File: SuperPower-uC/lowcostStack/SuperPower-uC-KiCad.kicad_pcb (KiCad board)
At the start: 4 copper layers, 92.2 x 45.2 mm, 105 parts, among them J1 Battery connector, J10 External NTC, J11 DNP, J2 Thermistor, J3 USB_B_Micro, J4 Solar in, J5 Conn_01x14_Female, J6 Conn_01x14_Female, J7 DNP, J8 regulator board, J9 MCU board, Q1 2N7002, Q2 2N7002, Q3 S8050, Q4 S8050, Q5 AO3401A, Q6 AO3401A, Q7 2N7002, Q8 2N7002, Q9 AO3401A, SW1 DNP, SW2 DNP, U1 AP9101CK6-ADTRG1, U10 FP6291LR, U11 ME6210A33P, U12 ME6210A33P, U13 ESP32-WROOM32, U14 W25Q32JVSS, U15 IP4220CZ6, U2 FS8205A, U3 LC709203FQH, U4 TP4056, U5 CH340G, U6 AMS1117-3.3, U7 PCF8563T, U8 XC6206P332MR, U9 TCA6408A, Y1 12MHZ, Y2 32.768KHz

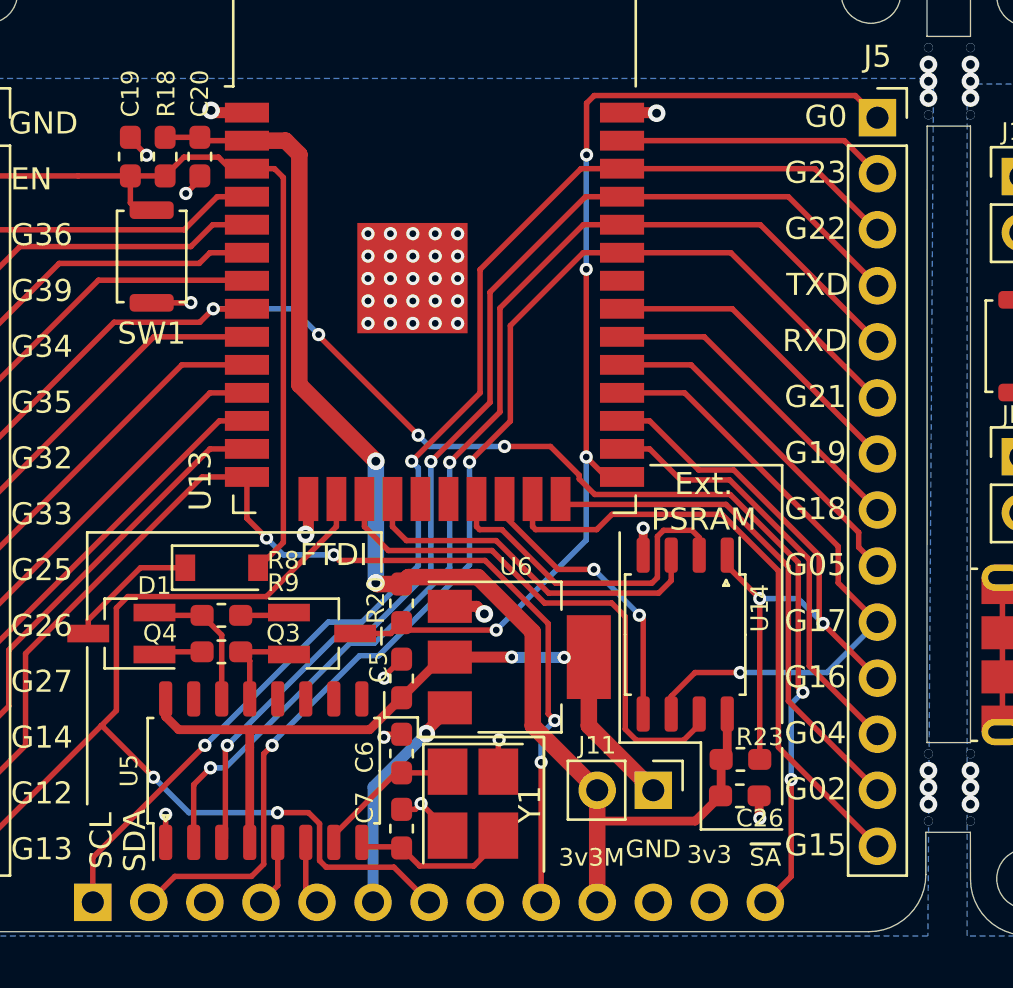
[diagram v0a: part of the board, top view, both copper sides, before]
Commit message: changed naming of usb to serial stuff and added led to mcu board
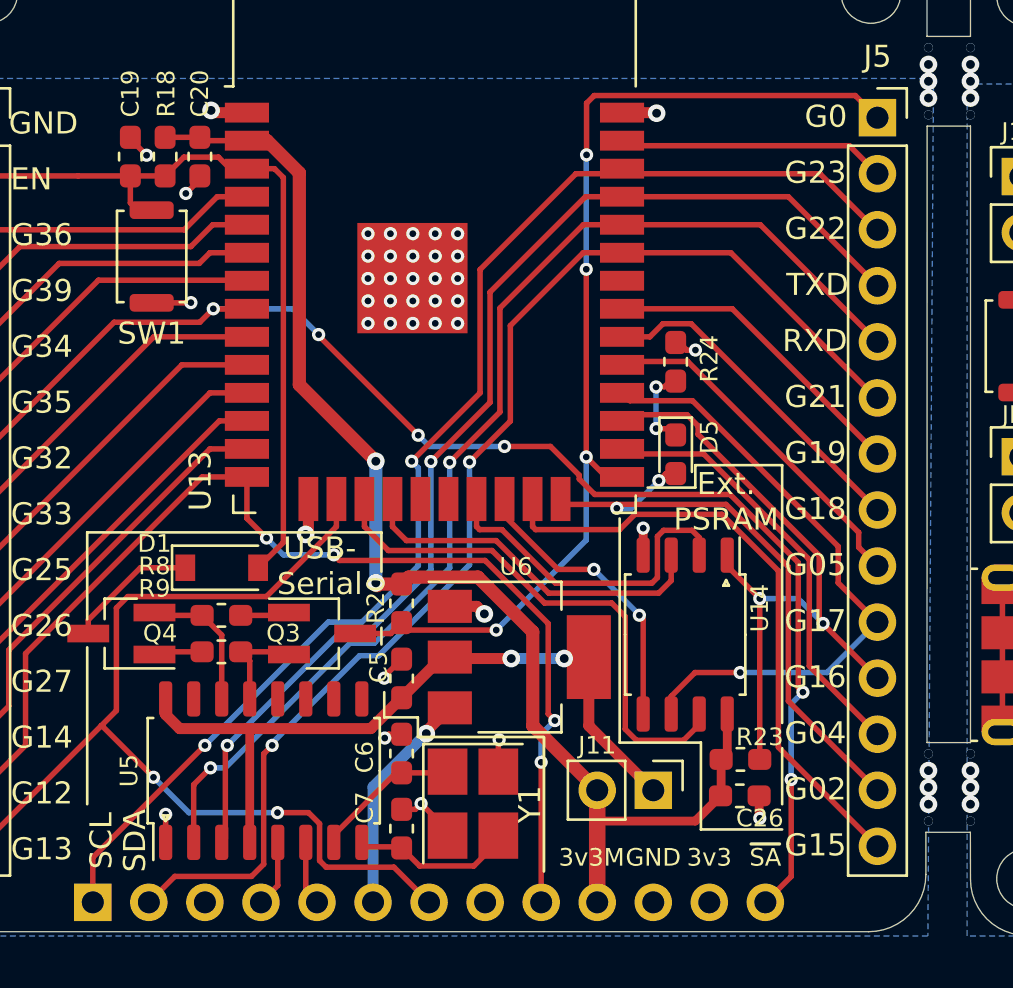
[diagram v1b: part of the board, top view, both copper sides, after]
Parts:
- added D5: LED, LED_SMD:LED_0603_1608Metric_Pad1.05x0.95mm_HandSolder, F.Cu at (135.4, 99.7)
- added R24: 100, Resistor_SMD:R_0603_1608Metric_Pad1.05x0.95mm_HandSolder, F.Cu at (135.4, 95.5)
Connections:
- net /MCU Module/3v3FTDI renamed /MCU Module/3v3_UART
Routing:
- net Net-(D5-Pad1): track 0.00 -> 3.89 mm, vias 0 -> 2
- net /MCU Module/IO2: track 23.8 -> 27.3 mm, vias 0 -> 2
- net GND: track 88.5 -> 89.6 mm, vias 80 -> 81
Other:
- board text added: "USB- Serial"
- board text removed: "FTDI"

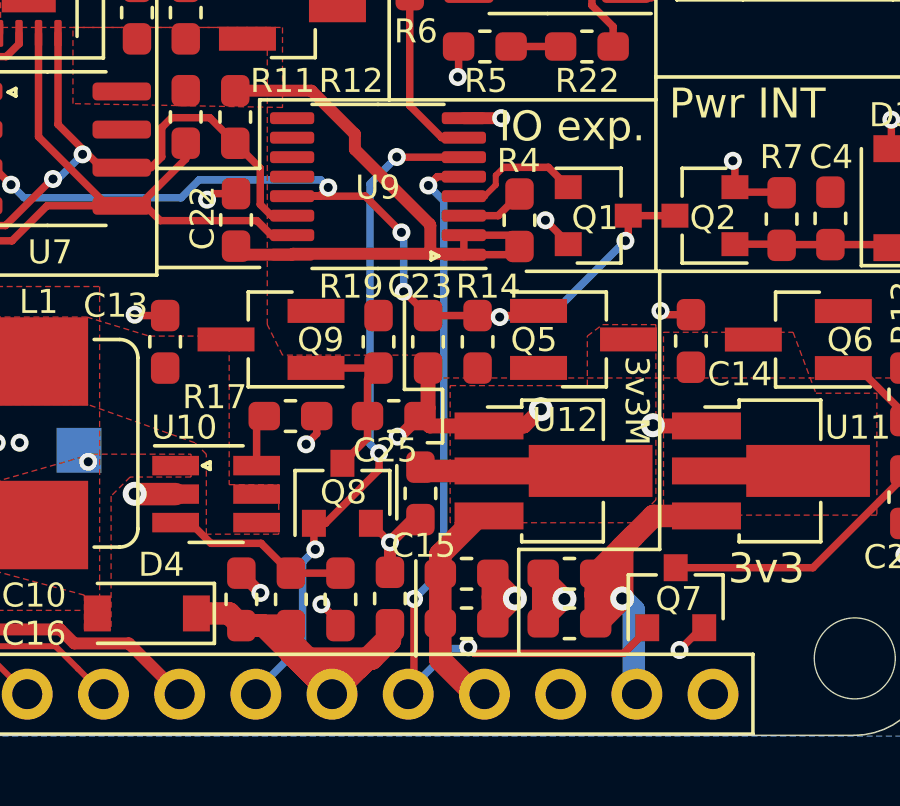
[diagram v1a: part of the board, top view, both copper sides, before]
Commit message: disconnected 5v_EN and 3v3_EN from the pin header on the regulator board
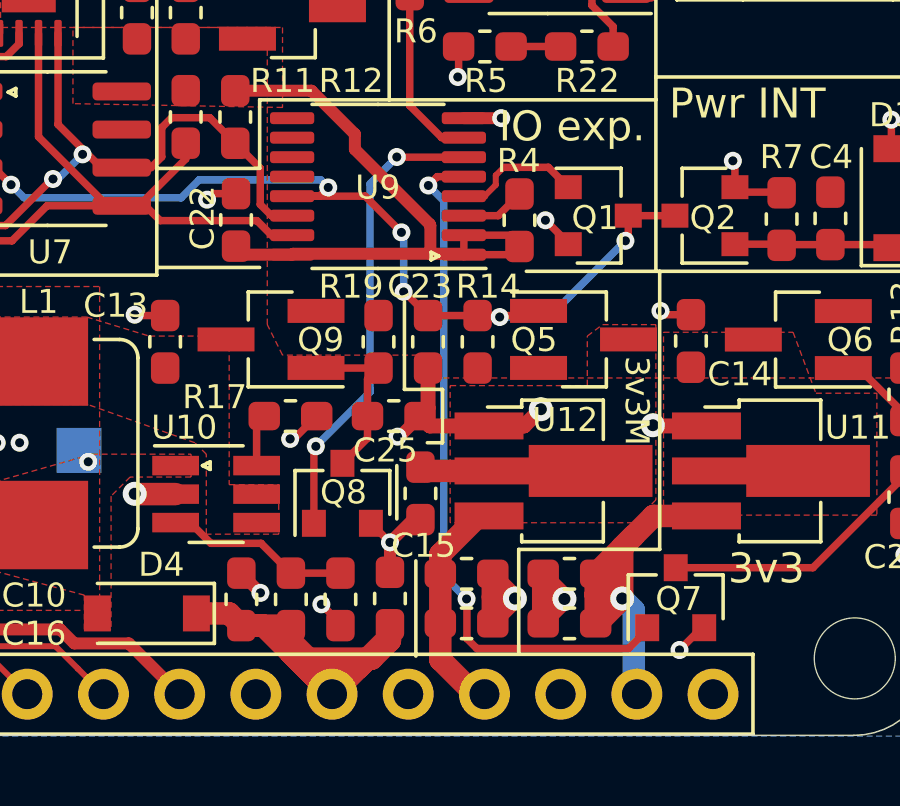
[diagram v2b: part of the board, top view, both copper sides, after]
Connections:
- J8 pad 7: 5V_EN -> Net-(J8-Pad7)
- J8 pad 9: 3v3_EN -> Net-(J8-Pad9)
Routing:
- net 5V_EN: track 22.6 -> 15.6 mm, vias 3 -> 2
- net 3v3_EN: track 28.3 -> 23.4 mm, vias 3 -> 2
